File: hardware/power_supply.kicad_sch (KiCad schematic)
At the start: 43 parts, among them U2 LM62440-Q1, U3 BD50FC0FP, U4 BD50FC0FP, U5 TLV743P, U6 TLV743P

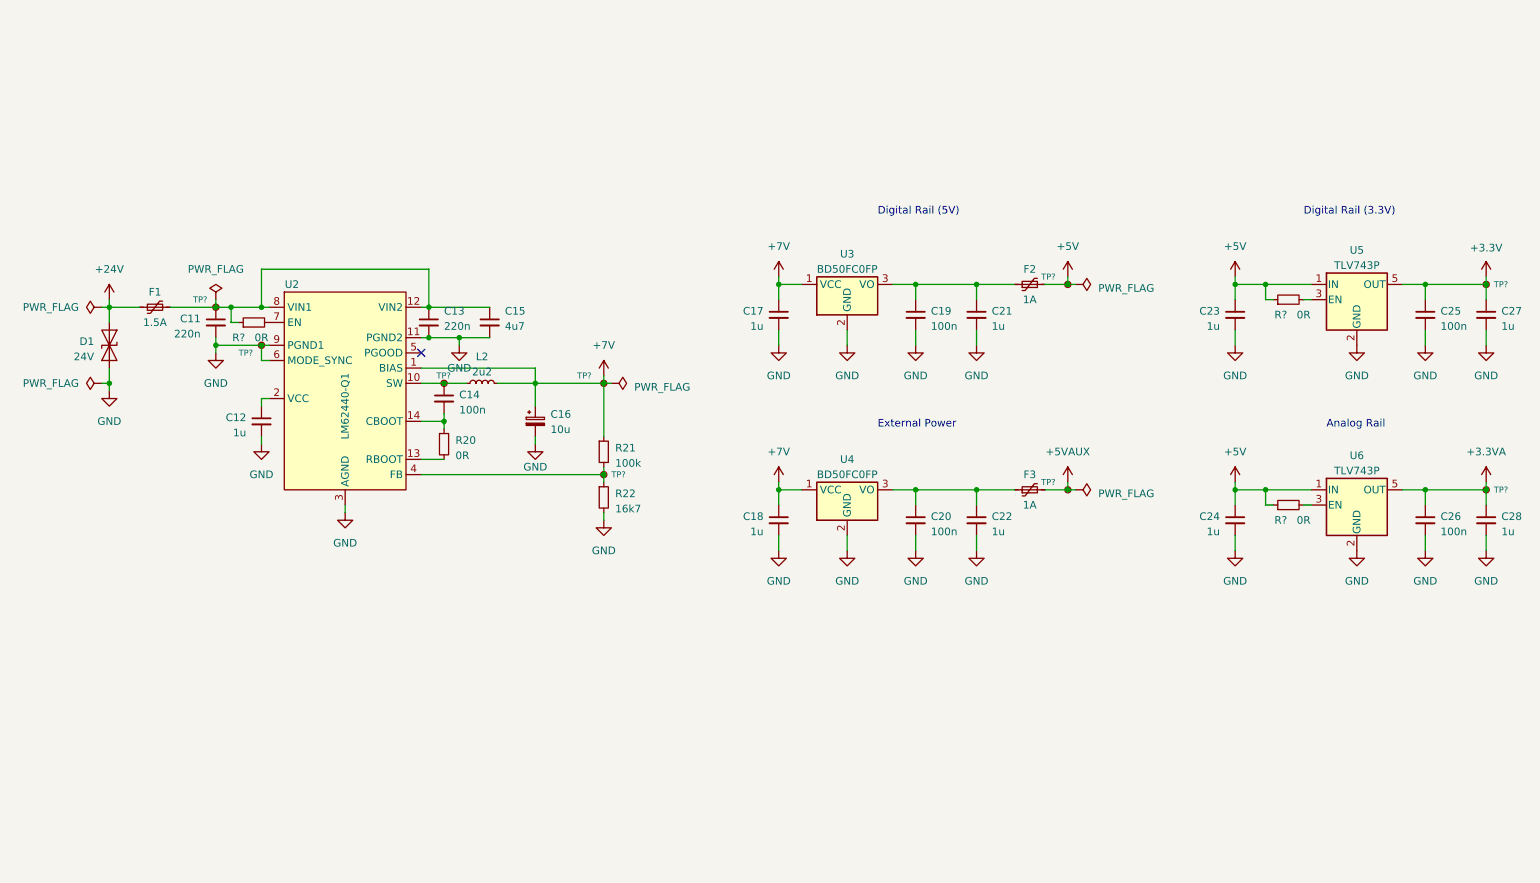
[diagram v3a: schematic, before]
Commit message: Improve the schematic according to the feedback
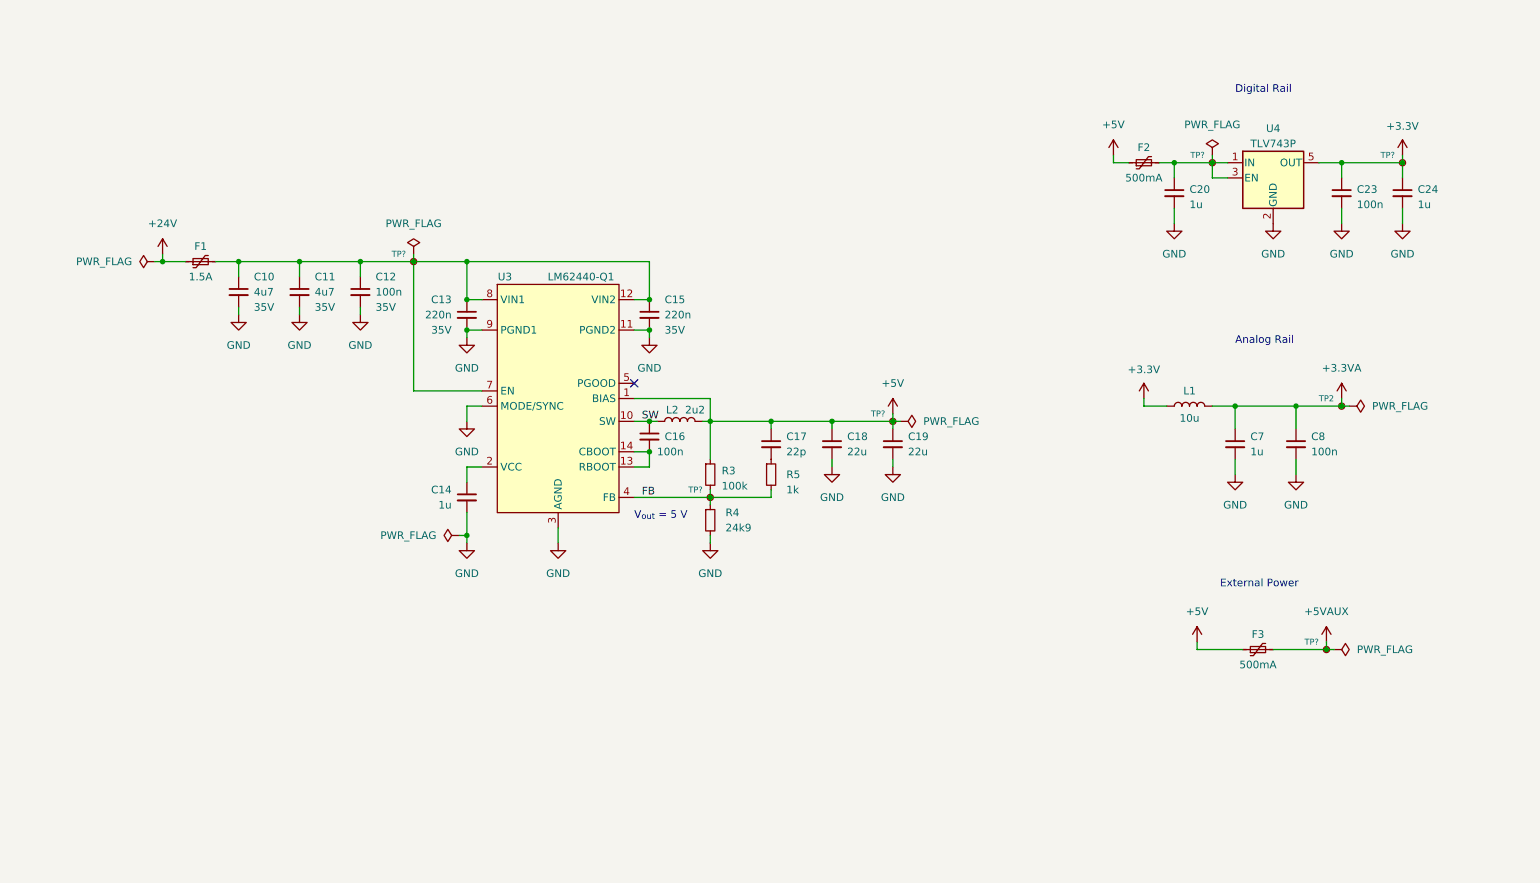
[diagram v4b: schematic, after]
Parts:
- removed C15: 4u7, Capacitor_SMD:CP_Elec_4x5.7, symbol Device:C_Small
- removed C16: 10u, Capacitor_SMD:CP_Elec_4x5.7, symbol Device:C_Polarized_Small
- removed C20, C26: 100n, Capacitor_SMD:C_0603_1608Metric, symbol Device:C_Small
- removed C21, C22, C24, C28: 1u, Capacitor_SMD:C_0603_1608Metric, symbol Device:C_Small
- removed D1: 24V, symbol Diode:SD24_SOD323
- removed R20, R? (x3): 0R, Resistor_SMD:R_0603_1608Metric, symbol Device:R_Small
- removed TP? (x4): TestPoint_Small, TestPoint:TestPoint_Pad_D1.0mm, symbol Connector:TestPoint_Small
- removed U3, U4: BD50FC0FP, Package_TO_SOT_SMD:TO-252-2, symbol Regulator_Linear:BD50FC0FP
- removed U6: TLV743P, Package_TO_SOT_SMD:SOT-23-5, symbol Regulator_Linear:TLV73330PDBV
- added C10: 4u7, Capacitor_SMD:C_0603_1608Metric, symbol Device:C_Small
- added C12, C8: 100n, Capacitor_SMD:C_0603_1608Metric, symbol Device:C_Small
- added C13: 220n, Capacitor_SMD:C_0603_1608Metric, symbol Device:C_Small
- added C7: 1u, Capacitor_SMD:C_0603_1608Metric, symbol Device:C_Small
- added L1: 10u, Inductor_SMD:L_0603_1608Metric, symbol Device:L
- added R5: 1k, Resistor_SMD:R_0603_1608Metric, symbol Device:R_Small
- added TP2, TP?: TestPoint_Small, TestPoint:TestPoint_Pad_D1.0mm, symbol Connector:TestPoint_Small
- C11: value 220n -> 4u7; Voltage (none) -> 35V
- C15: renamed from C13; Voltage (none) -> 35V
- C17: value 1u -> 22p
- C18: value 1u -> 22u
- C19: value 100n -> 22u
- F2, F3: value 1A -> 500mA
- L2: symbol Device:L_Small -> Device:L
- R4: renamed from R22; value 16k7 -> 24k9
- renumbered C12 to C14, C14 to C16, C23 to C20, C25 to C23, C27 to C24, R21 to R3, U2 to U3, U5 to U4
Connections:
- net +7V is gone; now on net +5V: C17.1, C18.1, L2.2, R3.1, TP?.1, U3.1 (BIAS)
- net +3.3V: now also L1.1
- net +3.3VA: now also C7.1, C8.1, L1.2, TP2.1
- net +5V: now also C19.1, F2.1, F3.1; no longer C20.1, F2.2, U4.1 (IN)
- net GND: now also C10.2, C12.2, C13.2, C7.2, C8.2; no longer C17.2
- net FB: now reaches R3.2, R4.1, TP?.1, U3.4 (FB)
- net FB: now also R5.2
- net SW: now reaches C16.1, L2.1, U3.10 (SW)
- net at C11.1, C15.1, F1.2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: now also U3.7 (EN), C10.1, C12.1, C13.1
- net at U3.13 (RBOOT): now also C16.2, U3.14 (CBOOT)
- net at U4.3 (EN): now also C20.1, F2.2, U4.1 (IN), TP?.1
- new net: C17.2, R5.1
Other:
- note added: "Digital Rail"
- note added: "V_{out} = 5 V"
- note removed: "Digital Rail (3.3V)"
- note removed: "Digital Rail (5V)"
- moved on the sheet: C14, C15, C16, C20, C23, C24, F1, F3, L2, R3, R4, TP?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

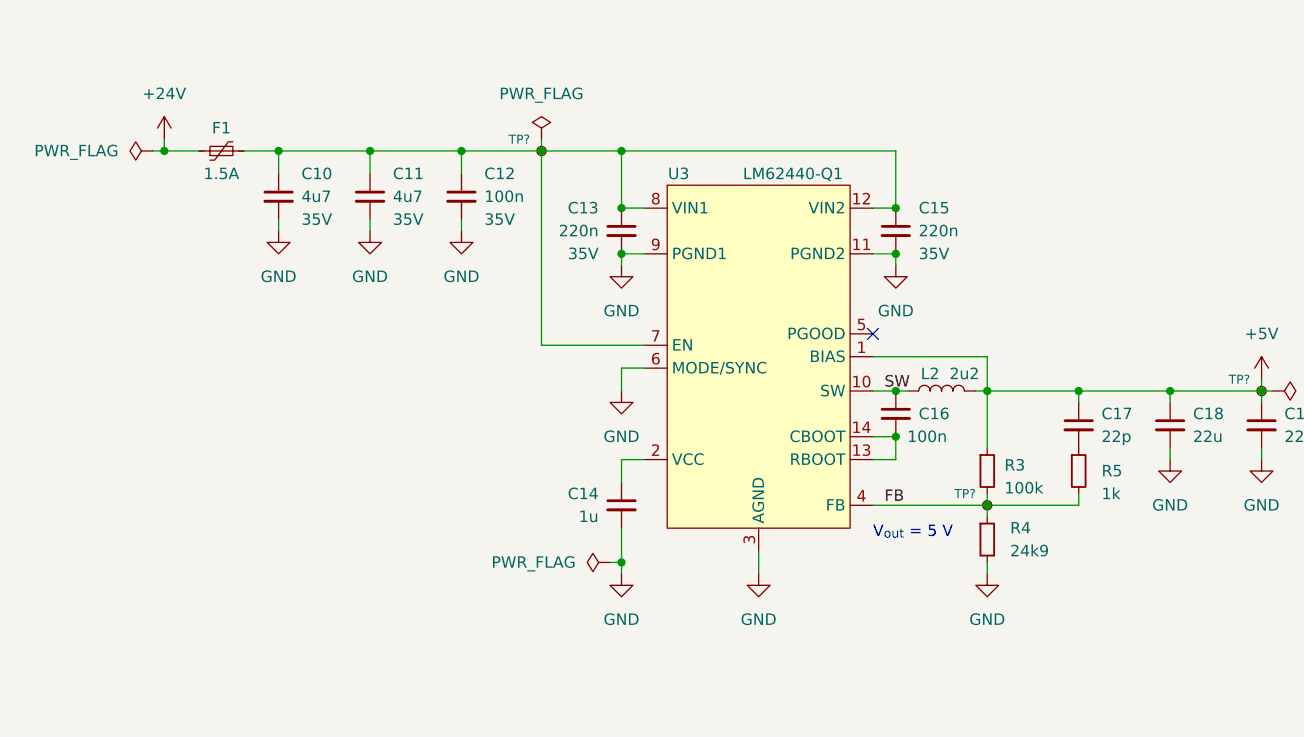
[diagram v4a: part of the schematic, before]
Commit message: Add high-side drivers to the fans and pumps
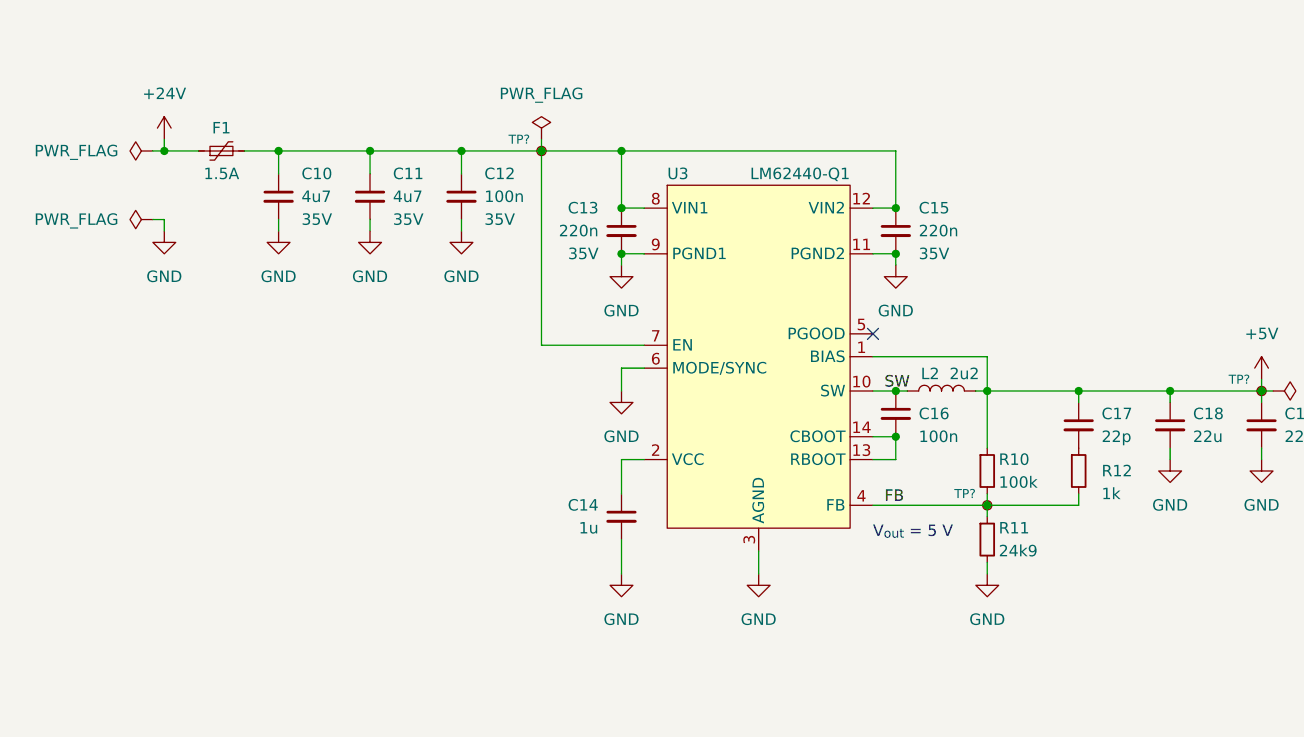
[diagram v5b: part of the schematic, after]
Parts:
- renumbered R3 to R10, R4 to R11, R5 to R12
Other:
- moved on the sheet: C14

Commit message: Use in-amps
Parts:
- renumbered R10 to R3, R11 to R4, R12 to R5
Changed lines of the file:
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@@
   (symbol (lib_id "Device:R_Small") (at 137.16 110.49 0) (unit 1)
     (in_bom yes) (on_board yes) (dnp no)
-    (property "Reference" "R10" (at 138.43 109.22 0)
+    (property "Reference" "R3" (at 138.43 109.22 0)
       (effects (font (size 1.27 1.27)) (justify left))
     )
@@
       (project "rearbox"
         (path "/b652b05a-4e3d-4ad1-b032-18886abe7d45/7045152e-d7a2-42d7-9b15-138e7f2928ca"
-          (reference "R10") (unit 1)
+          (reference "R3") (unit 1)
         )
       )
@@
   (symbol (lib_id "Device:R_Small") (at 137.16 118.11 0) (unit 1)
     (in_bom yes) (on_board yes) (dnp no)
-    (property "Reference" "R11" (at 138.43 116.84 0)
+    (property "Reference" "R4" (at 138.43 116.84 0)
       (effects (font (size 1.27 1.27)) (justify left))
     )
@@
       (project "rearbox"
         (path "/b652b05a-4e3d-4ad1-b032-18886abe7d45/7045152e-d7a2-42d7-9b15-138e7f2928ca"
-          (reference "R11") (unit 1)
+          (reference "R4") (unit 1)
         )
       )
@@
   (symbol (lib_id "Device:R_Small") (at 147.32 110.49 0) (unit 1)
     (in_bom yes) (on_board yes) (dnp no)
-    (property "Reference" "R12" (at 149.86 110.49 0)
+    (property "Reference" "R5" (at 149.86 110.49 0)
       (effects (font (size 1.27 1.27)) (justify left))
     )
@@
       (project "rearbox"
         (path "/b652b05a-4e3d-4ad1-b032-18886abe7d45/7045152e-d7a2-42d7-9b15-138e7f2928ca"
-          (reference "R12") (unit 1)
-        )
-      )
+          (reference "R5") (unit 1)
+        )
+      )

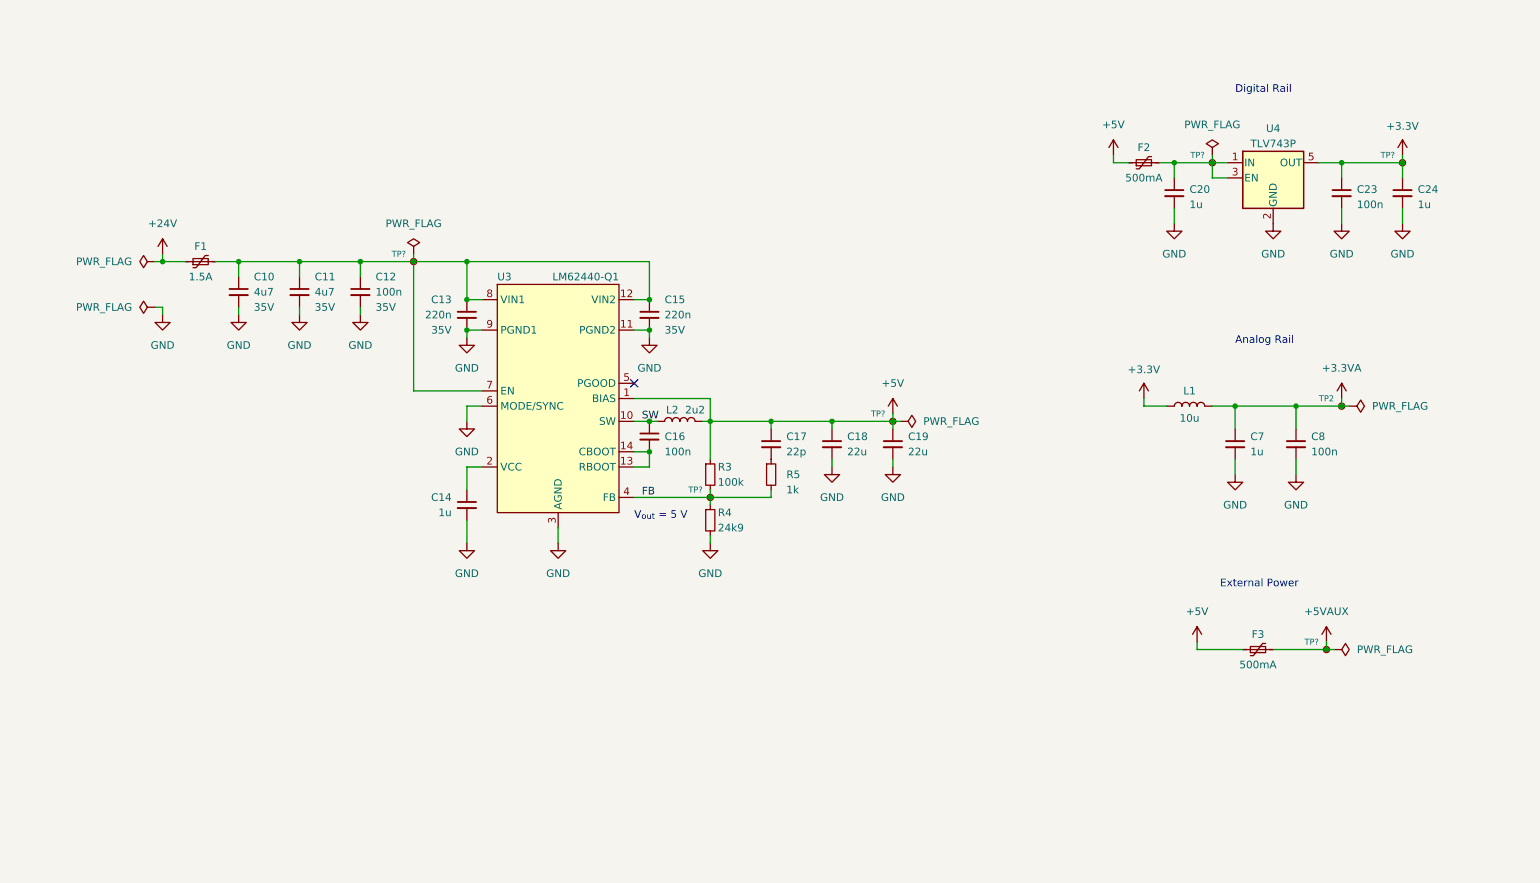
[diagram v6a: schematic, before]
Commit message: Improve the diagram based on the feedback
- add an input LC filter
- remove the USB connector
- add a programmer connector
- move optocouplers into a subsheet
- add a suspension tension meter IC
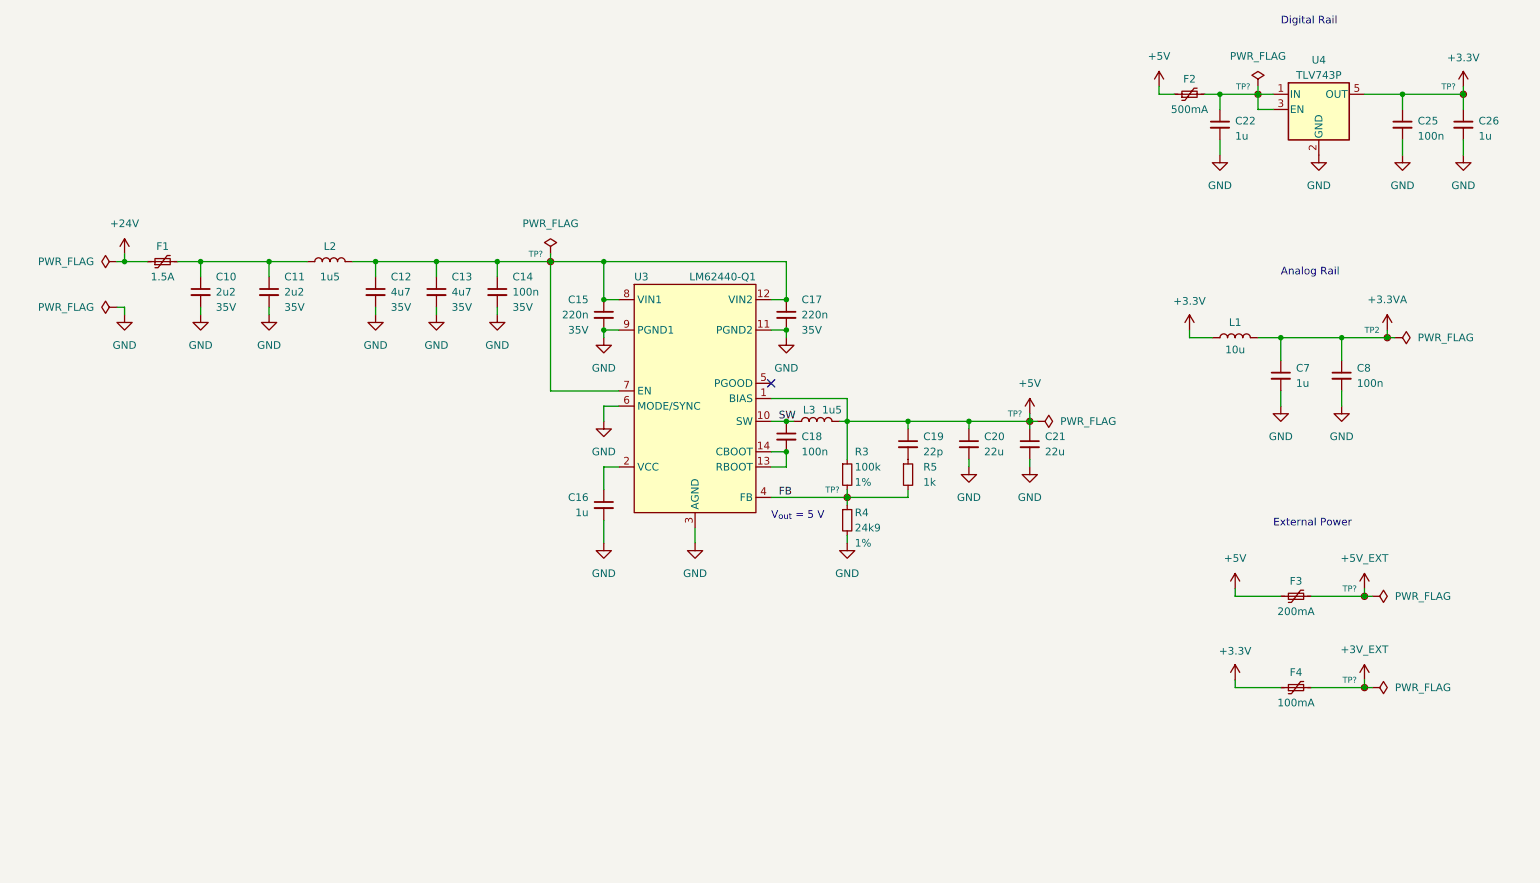
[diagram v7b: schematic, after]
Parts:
- added C10, C11: 2u2, Capacitor_SMD:C_0603_1608Metric, symbol Device:C_Small
- added F4: 100mA, Fuse:Fuse_1812_4532Metric, symbol Device:Polyfuse_Small
- added L2: 1u5, Inductor_SMD:L_Abracon_ASPI-4030S, symbol Device:L
- added TP?: TestPoint_Small, TestPoint:TestPoint_Pad_D1.0mm, symbol Connector:TestPoint_Small
- C12: renamed from C10; Rated Voltage (none) -> 35V; Voltage 35V -> (none)
- C13: renamed from C11; Rated Voltage (none) -> 35V; Voltage 35V -> (none)
- C14: renamed from C12; Rated Voltage (none) -> 35V; Voltage 35V -> (none)
- C15: renamed from C13; Rated Voltage (none) -> 35V; Voltage 35V -> (none)
- C17: renamed from C15; Rated Voltage (none) -> 35V; Voltage 35V -> (none)
- F1: footprint Fuse:Fuse_0603_1608Metric -> Fuse:Fuse_1812_4532Metric; Component (none) -> PTS181233V075
- F2: footprint Fuse:Fuse_0603_1608Metric -> Fuse:Fuse_1812_4532Metric; Component (none) -> PTS181216V050
- F3: value 500mA -> 200mA; footprint Fuse:Fuse_0603_1608Metric -> Fuse:Fuse_1812_4532Metric; Component (none) -> PTS181216V050
- L3: renamed from L2; value 2u2 -> 1u5
- R3, R4: Tolerance (none) -> 1%
- renumbered C14 to C16, C16 to C18, C17 to C19, C18 to C20, C19 to C21, C20 to C22, C23 to C25, C24 to C26
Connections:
- net +3.3V: now also F4.1
- net GND: now also C10.2, C11.2
- net at C12.1, C13.1, C14.1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: now also L2.2; no longer F1.2
- net +5VAUX renamed +5V_EXT
- new net: C10.1, C11.1, F1.2, L2.1
- new net +3V_EXT: F4.2, TP?.1
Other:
- title: (none) -> Power Supply
- moved on the sheet: C12, C13, C14, C15, C16, C17, C18, C19, C20, C21, C22, C25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
